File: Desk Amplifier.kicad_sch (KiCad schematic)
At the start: 43 parts, among them J1 AudioJack3, J2 AudioJack3, J3 AudioJack3, J4 AudioJack3, J5 Barrel_Jack, U1 OPA2134, U2 OPA2134, U3 OPA2134, U4 OPA2134

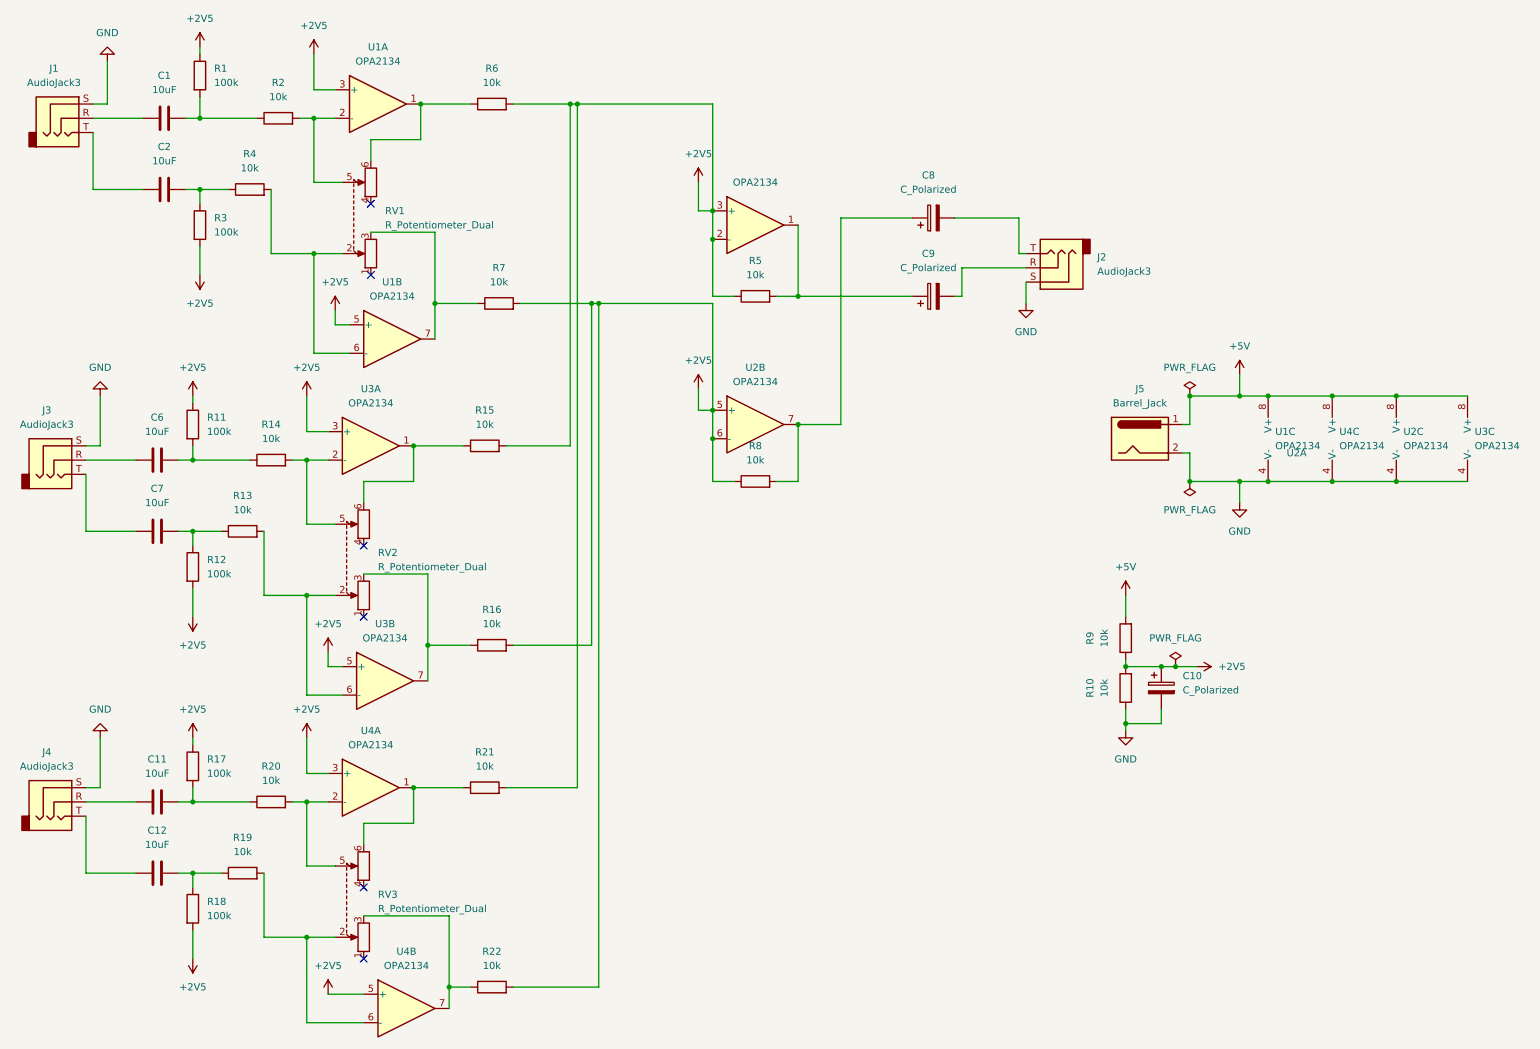
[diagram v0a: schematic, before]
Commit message: simplified version: passive input
no pre-amp
accept 180 phase shift
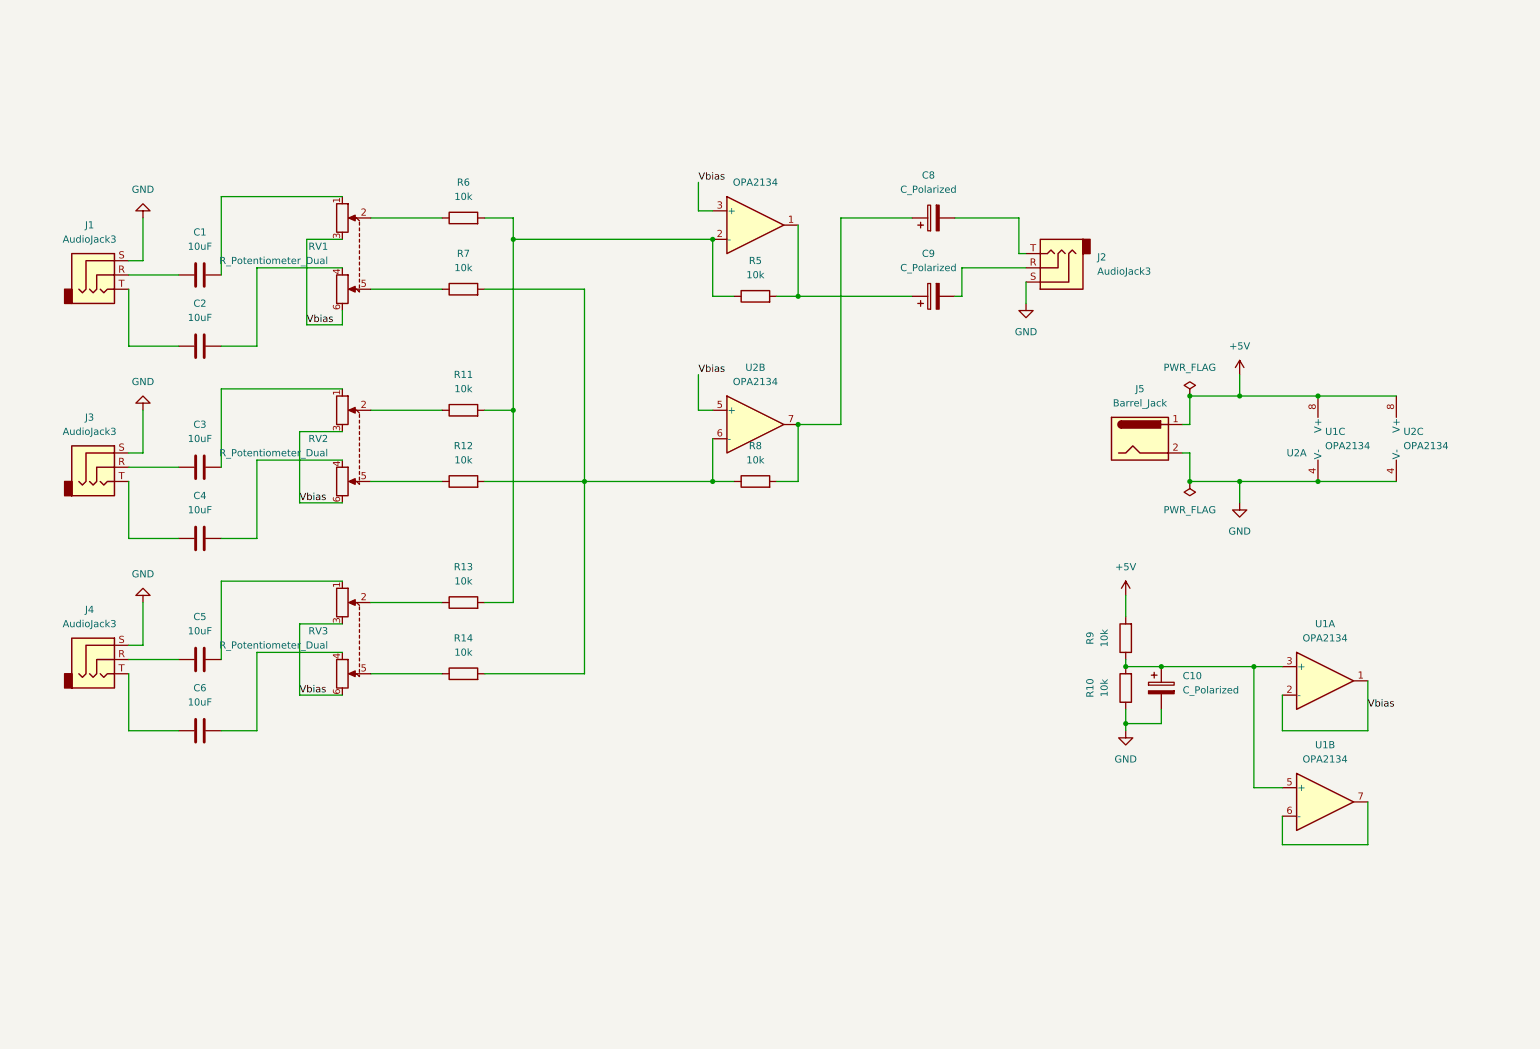
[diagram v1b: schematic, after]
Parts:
- removed C11, C12, C7: 10uF, Capacitor_THT:C_Disc_D10.0mm_W2.5mm_P5.00mm, symbol Device:C
- removed R1, R17, R18, R3: 100k, Resistor_THT:R_Axial_DIN0207_L6.3mm_D2.5mm_P7.62mm_Horizontal, symbol Device:R
- removed R15, R16, R19, R2, R20, R21, R22, R4: 10k, Resistor_THT:R_Axial_DIN0207_L6.3mm_D2.5mm_P7.62mm_Horizontal, symbol Device:R
- removed unit 1 of U1
- removed unit 2 of U1
- removed U3, U4: OPA2134, Package_DIP:DIP-8_W7.62mm, symbol Amplifier_Operational:OPA2134
- added C3, C4, C5: 10uF, Capacitor_THT:C_Disc_D10.0mm_W2.5mm_P5.00mm, symbol Device:C
- R11, R12: value 100k -> 10k
- U1: footprint Package_DIP:DIP-8_W7.62mm -> (none)
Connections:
- net at C1.2: now also RV1.1
- net at C2.2: now also RV1.4
- net at RV1.2: now also R6.1
- net at RV3.2: now also R13.1
- net Vbias: now reaches RV3.3
- net Vbias: now also RV1.3, RV1.6, RV2.3, RV2.6, RV3.6, U1.1, U1.2 (-), U2.3 (+), U2.5 (+)
- net at R14.2: now also R12.2, R7.2, R8.1, U2.6 (-); no longer RV2.5
- net at C6.1: now also J4.T; no longer J3.R
- net at RV3.5: now also R14.1
- net at J3.T: now also C4.1
- net at J4.R: now also C5.1
- net at R13.2: now also R11.2, R5.1, R6.2, U2.2 (-); no longer RV2.2
- net at R7.1: now also RV1.5; no longer RV1.3
- net at RV3.1: now also C5.2
- net at RV3.4: now also C6.2
- net at RV2.1: now also C3.2
- net at RV2.4: now also C4.2
- net at R12.1: now also RV2.5; no longer R13.1
- removed net +2V5: C10.1, R10.2, R11.1, R12.2, R5.1, R6.2, R7.2, R8.1, R9.1, U2.2 (-), U2.3 (+), U2.5 (+), U2.6 (-)
- new net: C10.1, R10.2, R9.1, U1.3 (+), U1.5 (+)
- new net: C3.1, J3.R
- new net: R11.1, RV2.2
- new net: U1.6 (-), U1.7
- no-connect marks 6 -> 0
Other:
- moved on the sheet: C1, C2, J1, R6, R7, RV1

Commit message: poc layout
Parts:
- C10, C8, C9: footprint (none) -> Capacitor_SMD:CP_Elec_3x5.3
- J2: footprint (none) -> Connector_Audio:Jack_3.5mm_CUI_SJ-3523-SMT_Horizontal
- U1, U2: footprint (none) -> Package_DIP:DIP-8-16_W7.62mm
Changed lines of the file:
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@@
 			)
 		)
-		(property "Footprint" ""
+		(property "Footprint" "Package_DIP:DIP-8-16_W7.62mm"
 			(at 146.05 87.63 0)
 			(hide yes)
@@
 			)
 		)
-		(property "Footprint" ""
+		(property "Footprint" "Connector_Audio:Jack_3.5mm_CUI_SJ-3523-SMT_Horizontal"
 			(at 199.39 59.69 0)
 			(hide yes)
@@
 			)
 		)
-		(property "Footprint" ""
+		(property "Footprint" "Capacitor_SMD:CP_Elec_3x5.3"
 			(at 181.61 63.8048 0)
 			(hide yes)
@@
 			)
 		)
-		(property "Footprint" ""
+		(property "Footprint" "Capacitor_SMD:CP_Elec_3x5.3"
 			(at 219.4052 138.43 0)
 			(hide yes)
@@
 		(in_pos_files yes)
 		(dnp no)
+		(fields_autoplaced yes)
 		(property "Reference" "U2"
-			(at 242.57 92.71 0)
+			(at 146.05 41.91 0)
 			(show_name no)
 			(do_not_autoplace no)
@@
 			)
 		)
-		(property "Footprint" ""
+		(property "Footprint" "Package_DIP:DIP-8-16_W7.62mm"
 			(at 146.05 52.07 0)
 			(hide yes)
@@
 			)
 		)
-		(property "Footprint" ""
+		(property "Footprint" "Capacitor_SMD:CP_Elec_3x5.3"
 			(at 181.61 49.8348 0)
 			(hide yes)
@@
 			)
 		)
-		(property "Footprint" ""
+		(property "Footprint" "Package_DIP:DIP-8-16_W7.62mm"
 			(at 247.65 154.94 0)
 			(hide yes)
@@
 			)
 		)
-		(property "Footprint" ""
+		(property "Footprint" "Package_DIP:DIP-8-16_W7.62mm"
 			(at 247.65 133.35 0)
 			(hide yes)
@@
 			)
 		)
-		(property "Footprint" ""
+		(property "Footprint" "Package_DIP:DIP-8-16_W7.62mm"
 			(at 248.92 90.17 0)
 			(hide yes)
@@
 			)
 		)
-		(property "Footprint" ""
+		(property "Footprint" "Package_DIP:DIP-8-16_W7.62mm"
 			(at 262.89 90.17 0)
 			(hide yes)

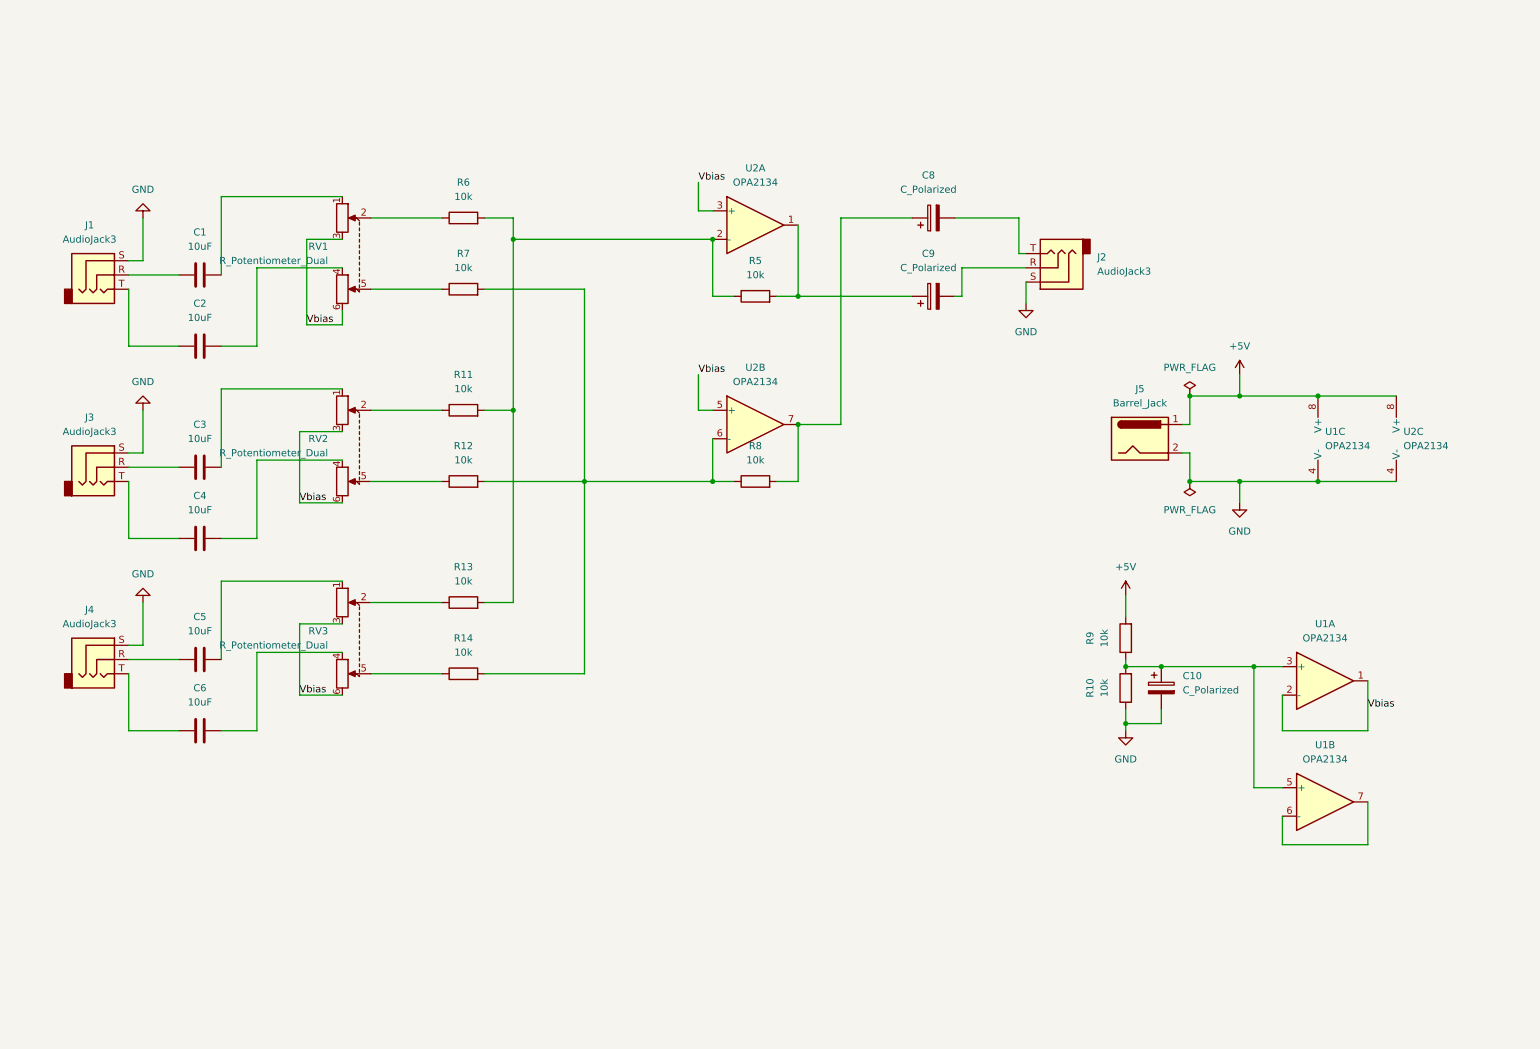
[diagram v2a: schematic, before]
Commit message: updated with real components
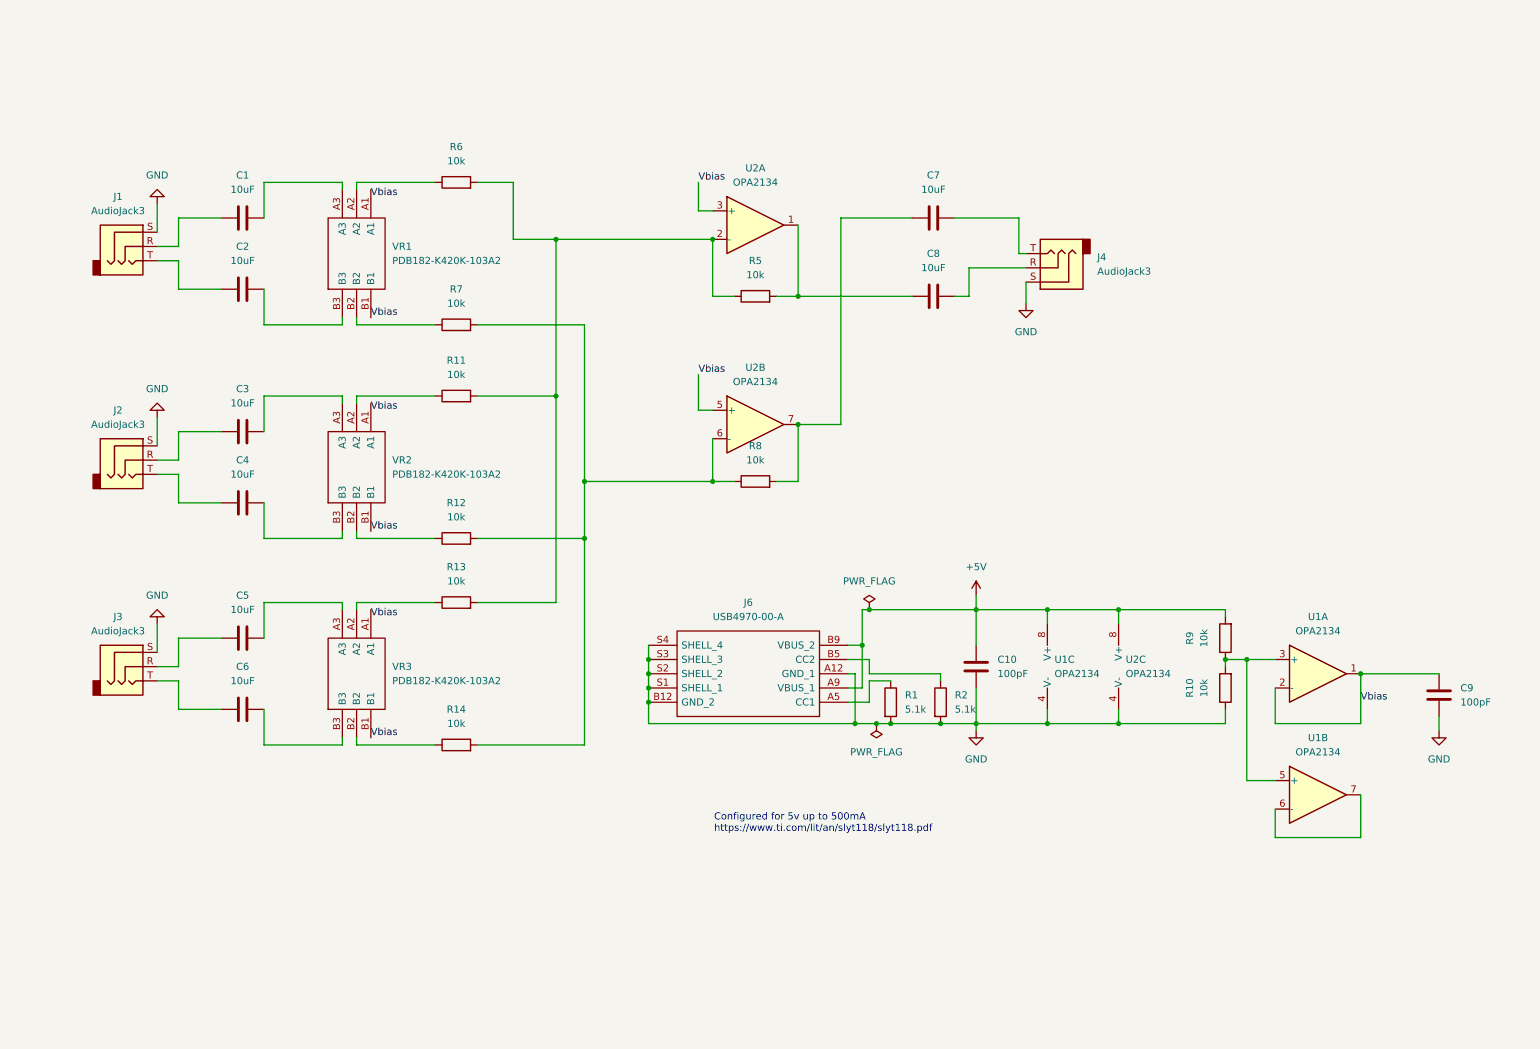
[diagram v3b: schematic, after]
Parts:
- removed C10, C8, C9: C_Polarized, Capacitor_SMD:CP_Elec_3x5.3, symbol Device:C_Polarized
- removed J4: AudioJack3, Connector_Audio:Jack_3.5mm_CUI_SJ-3523-SMT_Horizontal, symbol Connector_Audio:AudioJack3
- removed J5: Barrel_Jack, Connector_BarrelJack:BarrelJack_SwitchcraftConxall_RAPC10U_Horizontal, symbol Connector:Barrel_Jack
- removed RV1, RV2, RV3: R_Potentiometer_Dual, Potentiometer_THT:Potentiometer_Alps_RK097_Dual_Horizontal, symbol Device:R_Potentiometer_Dual
- added C10, C9: 100pF, Capacitor_THT:C_Disc_D10.0mm_W2.5mm_P5.00mm, symbol Device:C
- added C7, C8: 10uF, Capacitor_THT:C_Disc_D10.0mm_W2.5mm_P5.00mm, symbol Device:C
- added J2: AudioJack3, Connector_Audio:Jack_3.5mm_CUI_SJ-3523-SMT_Horizontal, symbol Connector_Audio:AudioJack3
- added J6: USB4970-00-A, Footprint Library:USB497000A, symbol Custom Library:USB4970-00-A
- added R1, R2: 5.1k, Resistor_THT:R_Axial_DIN0207_L6.3mm_D2.5mm_P7.62mm_Horizontal, symbol Device:R
- added unit 1 of U1
- added unit 3 of U1
- added VR1, VR2, VR3: PDB182-K420K-103A2, Footprint Library:PDB182K420P204A2, symbol Custom Library:PDB182-K420K-103A2
- U1, U2: footprint Package_DIP:DIP-8-16_W7.62mm -> Package_DIP:DIP-8_W7.62mm
- renumbered J2 to J4
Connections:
- net +5V: now also C10.2, J6.A9 (VBUS_1), J6.B9 (VBUS_2), U1.8 (V+); no longer U1.8 (V+)
- net GND: now also C10.1, C9.1, J2.S, J6.A12 (GND_1), J6.B12 (GND_2), J6.S1 (SHELL_1), J6.S2 (SHELL_2), J6.S3 (SHELL_3), J6.S4 (SHELL_4), R1.2, R2.2, U1.4 (V-); no longer U1.4 (V-)
- net Vbias: now also C9.2, U1.1, U1.2 (-), VR1.A1, VR1.B1, VR2.A1, VR2.B1, VR3.A1, VR3.B1; no longer U1.1, U1.2 (-)
- net at R5.2, U2.1: now also C8.1
- net at R8.2, U2.7: now also C7.1
- net at R10.2, R9.1, U1.5 (+): now also U1.3 (+); no longer U1.3 (+)
- net at C5.1: now also J3.R
- net at C6.1: now also J3.T
- net at C3.1: now also J2.R; no longer J3.R
- net at C3.2: now also VR2.A3
- net at C5.2: now also VR3.A3
- net at R11.1: now also VR2.A2
- net at C4.2: now also VR2.B3
- net at R12.1: now also VR2.B2
- net at C4.1: now also J2.T; no longer J3.T
- net at C2.2: now also VR1.B3
- net at J4.R: now also C8.2
- net at J4.T: now also C7.2
- net at C1.2: now also VR1.A3
- net at R7.1: now also VR1.B2
- net at R13.1: now also VR3.A2
- net at C6.2: now also VR3.B3
- net at R14.1: now also VR3.B2
- net at R6.1: now also VR1.A2
- new net: J6.A5 (CC1), R1.1
- new net: J6.B5 (CC2), R2.1
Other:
- note added: "Configured for 5v up to 500mA https://www.ti.com/lit/an/slyt118/slyt118.pdf"
- moved on the sheet: C1, C2, J1, R10, R11, R12, R13, R14, R6, R7, R9, U1B

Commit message: use STX-3000 for 2.5mm jack connection + routing
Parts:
- removed J1, J2, J3, J4: AudioJack3, Connector_Audio:Jack_3.5mm_CUI_SJ-3523-SMT_Horizontal, symbol Connector_Audio:AudioJack3
- added J1, J2, J3, J4: STX-3000, Footprint Library:STX3000, symbol Custom Library:STX-3000
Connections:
- net GND: now also J1.1, J2.1, J3.1, J4.1
- net at C4.1: now also J2.3
- net at C8.2: now also J4.2
- net at C5.1: now also J3.2
- net at C6.1: now also J3.3
- net at C2.1: now also J1.3
- net at C7.2: now also J4.3
- net at C1.1: now also J1.2
- net at C3.1: now also J2.2
